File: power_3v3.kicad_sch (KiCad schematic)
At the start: 20 parts, among them U12 TPS7A2033PDBVR, U7 TPS62913RPUR

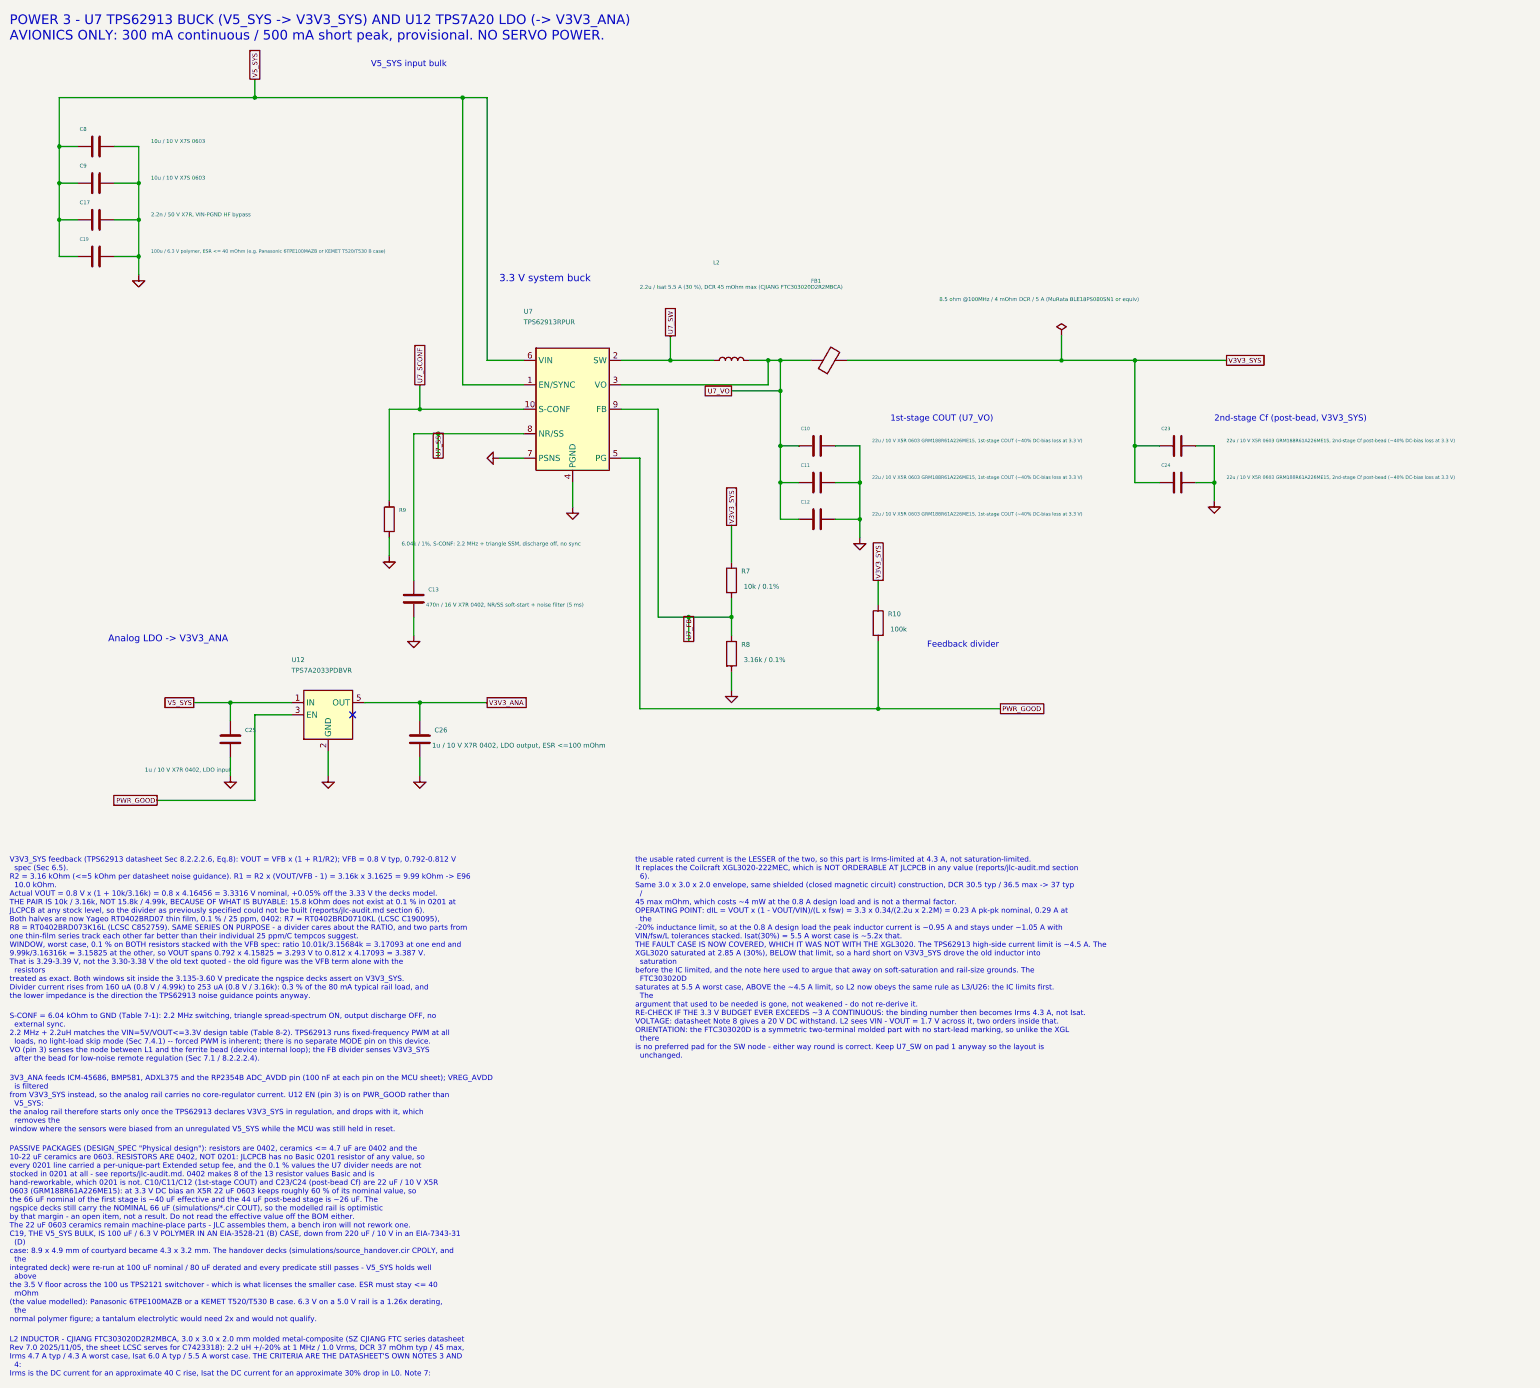
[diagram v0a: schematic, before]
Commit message: Power tree: 5 V-in from an external BEC; drop pack buck, TPS2121 mux, TPS62913 stage and USB ESD
Reverses the "pack-powered from the ESC" decision, which was made without
the owner's agreement and inverted the stated requirement (5 V in from a
BEC between the ESC and the FC, so any 2-6S BEC or a 1S boost works
upstream). 140 -> 116 parts; JLC 46 -> 32 LCSC parts, 29 -> 17 Extended.

- J3 ESC row 1x08 -> 1x09: pad 7 5V_IN, pad 8 GND, pad 9 VBAT (sense only,
  feeds the R27/R28/C48 divider on GPIO41; no zone, dropped from Power class)
- USB/5V OR: Q1 AO3401A (gate on USB_VBUS, 100k pull-down) + D1 1N5819WS,
  both JLC Basic. IO-block 5 V rows, C19, C20, C21 move ahead of the FET
  onto 5V_IN; V5_SYS feeds only U7, U12 and the status LED
- 3.3 V system rail: AP63203WU-7 fixed 3.3 V buck on its datasheet
  application circuit (DS41326 Table 2; 4.7 uH FTC404030S reused per sec. 10)
  replaces TPS62913 + FB1 + 0.1 % divider + two-stage filter. JLC Basic has
  no synchronous buck at all, so this one Extended part is accepted
- U12 TPS7A2033 analog LDO kept; EN now tied to V3V3_SYS (PWR_GOOD gone)
- PWR_SRC_ST gone, GPIO37 freed (no-connect); R10 becomes the MCU_RUN pull-up
- U8 USBLC6 (Extended) removed; D+/D- straight to the 27 R series resistors
- ngspice decks that modelled the removed chain retired to
  simulations/superseded/; run_power_checks.py reports RETIRED, not PASS
- DESIGN_SPEC decisions, README, LIBRARIES, PINOUT, BOM, JLC files and
  reports regenerated

Also carries the pre-session working-tree changes (grommet footprint
MountingHole_4.0mm_Grommet -> _Pad_Via, setup_pcb floorplan, JLC tooling).

Verified: ERC 0 violations; check_power_netlist PASS (5V_IN/V5_SYS/VBAT
membership asserted); setup_pcb 0 fit/geometry problems; stitch 150 vias;
DRC 5 silk_edge_clearance warnings only (board unrouted by design);
audit_footprints 116/116; JLC live audit 0 unresolved fitted parts;
generators idempotent modulo UUIDs.

Co-Authored-By: Claude Fable 5.1 <noreply@anthrop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
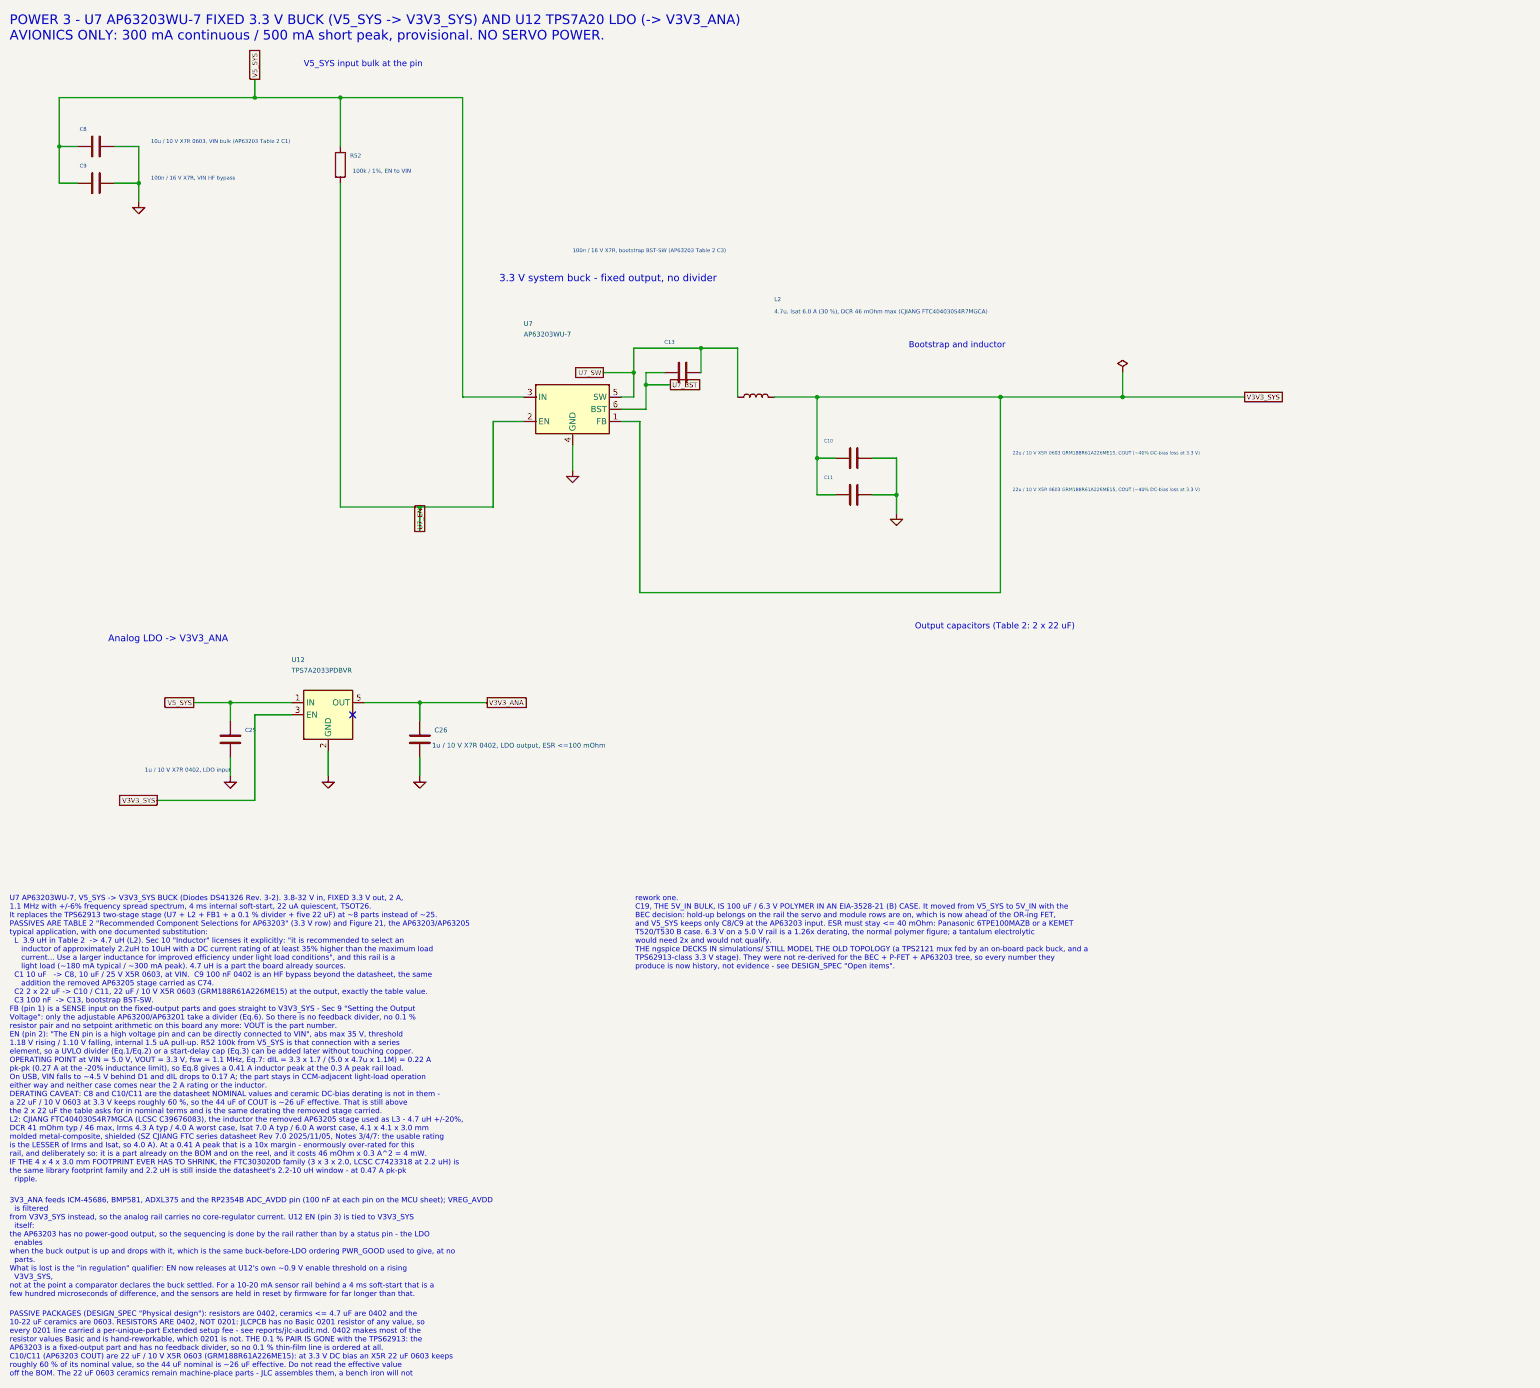
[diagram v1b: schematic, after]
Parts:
- removed C12: 22u / 10 V X5R 0603 GRM188R61A226ME15, 1st-stage 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, Capacitor_SMD:C_0603_1608Metric, symbol Device:C
- removed C17: 2.2n / 50 V X7R, VIN-PGND HF bypass, Capacitor_SMD:C_0402_1005Metric, symbol Device:C
- removed C19: 100u / 6.3 V polymer, ESR <= 40 mOhm (e.g. Panaso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, Capacitor_Tantalum_SMD:CP_EIA-3528-21_Kemet-B, symbol Device:C
- removed C23, C24: 22u / 10 V X5R 0603 GRM188R61A226ME15, 2nd-stage 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, Capacitor_SMD:C_0603_1608Metric, symbol Device:C
- removed FB1: 8.5 ohm @100MHz / 4 mOhm DCR / 5 A (MuRata BLE18P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, Inductor_SMD:L_0603_1608Metric, symbol Device:FerriteBead
- removed R10: 100k, Resistor_SMD:R_0402_1005Metric, symbol Device:R
- removed R7: 10k / 0.1%, Resistor_SMD:R_0402_1005Metric, symbol Device:R
- removed R8: 3.16k / 0.1%, Resistor_SMD:R_0402_1005Metric, symbol Device:R
- removed R9: 6.04k / 1%, S-CONF: 2.2 MHz + triangle SSM, disch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, Resistor_SMD:R_0402_1005Metric, symbol Device:R
- added R52: 100k / 1%, EN to VIN, Resistor_SMD:R_0402_1005Metric, symbol Device:R
- C10, C11: value 22u / 10 V X5R 0603 GRM188R61A226ME15, 1st-stage COUT (~40% DC-bias loss at 3.3 V) -> 22u / 10 V X5R 0603 GRM188R61A226ME15, COUT (~40% DC-bias loss at 3.3 V)
- C13: value 470n / 16 V X7R 0402, NR/SS soft-start + noise filter (5 ms) -> 100n / 16 V X7R, bootstrap BST-SW (AP63203 Table 2 C3); LCSC C471404 -> C1525
- C8: value 10u / 10 V X7S 0603 -> 10u / 10 V X7R 0603, VIN bulk (AP63203 Table 2 C1)
- C9: value 10u / 10 V X7S 0603 -> 100n / 16 V X7R, VIN HF bypass; footprint Capacitor_SMD:C_0603_1608Metric -> Capacitor_SMD:C_0402_1005Metric; LCSC C96446 -> C1525
- L2: value 2.2u / Isat 5.5 A (30 %), DCR 45 mOhm max (CJIANG FTC303020D2R2MBCA) -> 4.7u, Isat 6.0 A (30 %), DCR 46 mOhm max (CJIANG FTC404030S4R7MGCA); footprint MARV_Packages:L_Changjiang_FTC303020D -> MARV_Packages:L_Changjiang_FTC404030S; LCSC C7423318 -> C39676083
- U7: value TPS62913RPUR -> AP63203WU-7; footprint MARV_Packages:Texas_RPU0010A_VQFN-HR-10_2x2mm_P0.5mm -> Package_TO_SOT_SMD:TSOT-23-6; symbol Regulator_Switching:TPS62913 -> Regulator_Switching:AP63203WU; LCSC C5189914 -> C780769
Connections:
- net GND: no longer C13.2, U7.7 (PSNS)
- net U7_SW: now also C13.2, U7.5 (SW); no longer U7.2 (SW)
- net V3V3_SYS: now also C10.1, C11.1, L2.2, U12.3 (EN), U7.1 (FB)
- net V5_SYS: now also U7.3 (IN), R52.1; no longer U7.1 (EN/SYNC), U7.6 (VIN)
- removed net PWR_GOOD: U12.3 (EN), U7.5 (PG)
- removed net U7_FB: U7.9 (FB)
- removed net U7_SCONF: U7.10 (S-CONF)
- net U7_SS renamed U7_BST
- net U7_BST: now also U7.6 (BST); no longer U7.8 (NR/SS)
- removed net U7_VO: C10.1, C11.1, L2.2, U7.3 (VO)
- new net U7_EN: R52.2, U7.2 (EN)
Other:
- note added: "3.3 V system buck - fixed output, no divider"
- note added: "3V3_ANA feeds ICM-45686, BMP581, ADXL375 and the RP2354B ADC_AVDD pin (100 nF at each pin on the MCU sheet); VREG_AVDD is filtered from V3V3_SYS instead, so the analog rail carries no core-regulator current. U12 EN (pin 3) is tied to V3V3_SYS itself: the AP63203 has no power-good output, so the sequencing is done by the rail rather than by a status pin - the LDO enables when the buck output is up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"
- note added: "Bootstrap and inductor"
- note added: "Output capacitors (Table 2: 2 x 22 uF)"
- note added: "PASSIVE PACKAGES (DESIGN_SPEC "Physical design"): resistors are 0402, ceramics <= 4.7 uF are 0402 and the 10-22 uF ceramics are 0603. RESISTORS ARE 0402, NOT 0201: JLCPCB has no Basic 0201 resistor of any value, so every 0201 line carried a per-unique-part Extended setup fee - see reports/jlc-audit.md. 0402 makes most of the resistor values Basic and is hand-reworkable, which 0201 is not. THE 0.1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"
- note added: "POWER 3 - U7 AP63203WU-7 FIXED 3.3 V BUCK (V5_SYS -> V3V3_SYS) AND U12 TPS7A20 LDO (-> V3V3_ANA) AVIONICS ONLY: 300 mA continuous / 500 mA short peak, provisional. NO SERVO POWER."
- note added: "U7 AP63203WU-7, V5_SYS -> V3V3_SYS BUCK (Diodes DS41326 Rev. 3-2). 3.8-32 V in, FIXED 3.3 V out, 2 A, 1.1 MHz with +/-6% frequency spread spectrum, 4 ms internal soft-start, 22 uA quiescent, TSOT26. It replaces the TPS62913 two-stage stage (U7 + L2 + FB1 + a 0.1 % divider + five 22 uF) at ~8 parts instead of ~25. PASSIVES ARE TABLE 2 "Recommended Component Selections for AP63203" (3.3 V row) and 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"
- note added: "V5_SYS input bulk at the pin"
- note added: "rework one. C19, THE 5V_IN BULK, IS 100 uF / 6.3 V POLYMER IN AN EIA-3528-21 (B) CASE. It moved from V5_SYS to 5V_IN with the BEC decision: hold-up belongs on the rail the servo and module rows are on, which is now ahead of the OR-ing FET, and V5_SYS keeps only C8/C9 at the AP63203 input. ESR must stay <= 40 mOhm: Panasonic 6TPE100MAZB or a KEMET T520/T530 B case. 6.3 V on a 5.0 V rail is a 1.26x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"
- note removed: "1st-stage COUT (U7_VO)"
- note removed: "2nd-stage Cf (post-bead, V3V3_SYS)"
- note removed: "3.3 V system buck"
- note removed: "3V3_ANA feeds ICM-45686, BMP581, ADXL375 and the RP2354B ADC_AVDD pin (100 nF at each pin on the MCU sheet); VREG_AVDD is filtered from V3V3_SYS instead, so the analog rail carries no core-regulator current. U12 EN (pin 3) is on PWR_GOOD rather than V5_SYS: the analog rail therefore starts only once the TPS62913 declares V3V3_SYS in regulation, and drops with it, which removes the window where th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"
- note removed: "Feedback divider"
- note removed: "L2 INDUCTOR - CJIANG FTC303020D2R2MBCA, 3.0 x 3.0 x 2.0 mm molded metal-composite (SZ CJIANG FTC series datasheet Rev 7.0 2025/11/05, the sheet LCSC serves for C7423318): 2.2 uH +/-20% at 1 MHz / 1.0 Vrms, DCR 37 mOhm typ / 45 max, Irms 4.7 A typ / 4.3 A worst case, Isat 6.0 A typ / 5.5 A worst case. THE CRITERIA ARE THE DATASHEET'S OWN NOTES 3 AND 4: Irms is the DC current for an approximate 40 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"
- note removed: "PASSIVE PACKAGES (DESIGN_SPEC "Physical design"): resistors are 0402, ceramics <= 4.7 uF are 0402 and the 10-22 uF ceramics are 0603. RESISTORS ARE 0402, NOT 0201: JLCPCB has no Basic 0201 resistor of any value, so every 0201 line carried a per-unique-part Extended setup fee, and the 0.1 % values the U7 divider needs are not stocked in 0201 at all - see reports/jlc-audit.md. 0402 makes 8 of the 1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"
- note removed: "POWER 3 - U7 TPS62913 BUCK (V5_SYS -> V3V3_SYS) AND U12 TPS7A20 LDO (-> V3V3_ANA) AVIONICS ONLY: 300 mA continuous / 500 mA short peak, provisional. NO SERVO POWER."
- note removed: "S-CONF = 6.04 kOhm to GND (Table 7-1): 2.2 MHz switching, triangle spread-spectrum ON, output discharge OFF, no external sync. 2.2 MHz + 2.2uH matches the VIN=5V/VOUT<=3.3V design table (Table 8-2). TPS62913 runs fixed-frequency PWM at all loads, no light-load skip mode (Sec 7.4.1) -- forced PWM is inherent; there is no separate MODE pin on this device. VO (pin 3) senses the node between L1 and t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"
- note removed: "V3V3_SYS feedback (TPS62913 datasheet Sec 8.2.2.2.6, Eq.8): VOUT = VFB x (1 + R1/R2); VFB = 0.8 V typ, 0.792-0.812 V spec (Sec 6.5). R2 = 3.16 kOhm (<=5 kOhm per datasheet noise guidance). R1 = R2 x (VOUT/VFB - 1) = 3.16k x 3.1625 = 9.99 kOhm -> E96 10.0 kOhm. Actual VOUT = 0.8 V x (1 + 10k/3.16k) = 0.8 x 4.16456 = 3.3316 V nominal, +0.05% off the 3.33 V the decks model. THE PAIR IS 10k / 3.16k, 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"
- note removed: "V5_SYS input bulk"
- note removed: "the usable rated current is the LESSER of the two, so this part is Irms-limited at 4.3 A, not saturation-limited. It replaces the Coilcraft XGL3020-222MEC, which is NOT ORDERABLE AT JLCPCB in any value (reports/jlc-audit.md section 6). Same 3.0 x 3.0 x 2.0 envelope, same shielded (closed magnetic circuit) construction, DCR 30.5 typ / 36.5 max -> 37 typ / 45 max mOhm, which costs ~4 mW at the 0.8 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"
- moved on the sheet: C10, C11, C13, L2
